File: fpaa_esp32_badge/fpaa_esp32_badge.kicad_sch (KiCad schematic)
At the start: 41 parts, among them J1 Conn_01x04, J11 Conn_01x05, J16 Conn_01x12, J2 Conn_01x04, J21 Conn_01x02, J22 Conn_01x03, J3 Conn_01x04, J4 Conn_01x04, J5 USB_C_Receptacle_USB2.0, J6 Micro_SD_Card_Det1, SW1 SW_Push, SW2 SW_Push, SW3 SW_Push, X1 SG-5032CAN

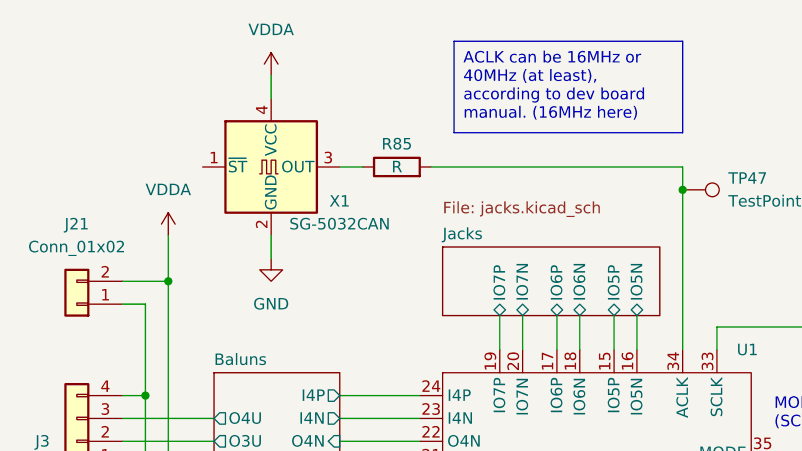
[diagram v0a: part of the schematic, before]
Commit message: added pdf and corrected some part values
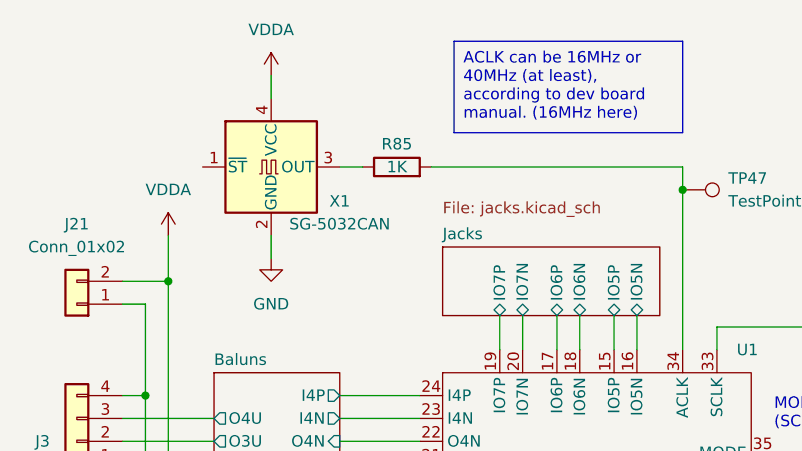
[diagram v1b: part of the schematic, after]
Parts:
- R85: value R -> 1K
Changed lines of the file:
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@@
       (effects (font (size 1.27 1.27)))
     )
-    (property "Value" "R" (at 55.88 31.75 90)
+    (property "Value" "1K" (at 55.88 31.75 90)
       (effects (font (size 1.27 1.27)))
     )
